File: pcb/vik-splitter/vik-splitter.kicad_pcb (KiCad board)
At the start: 2 copper layers, 25 x 25 mm, 7 parts

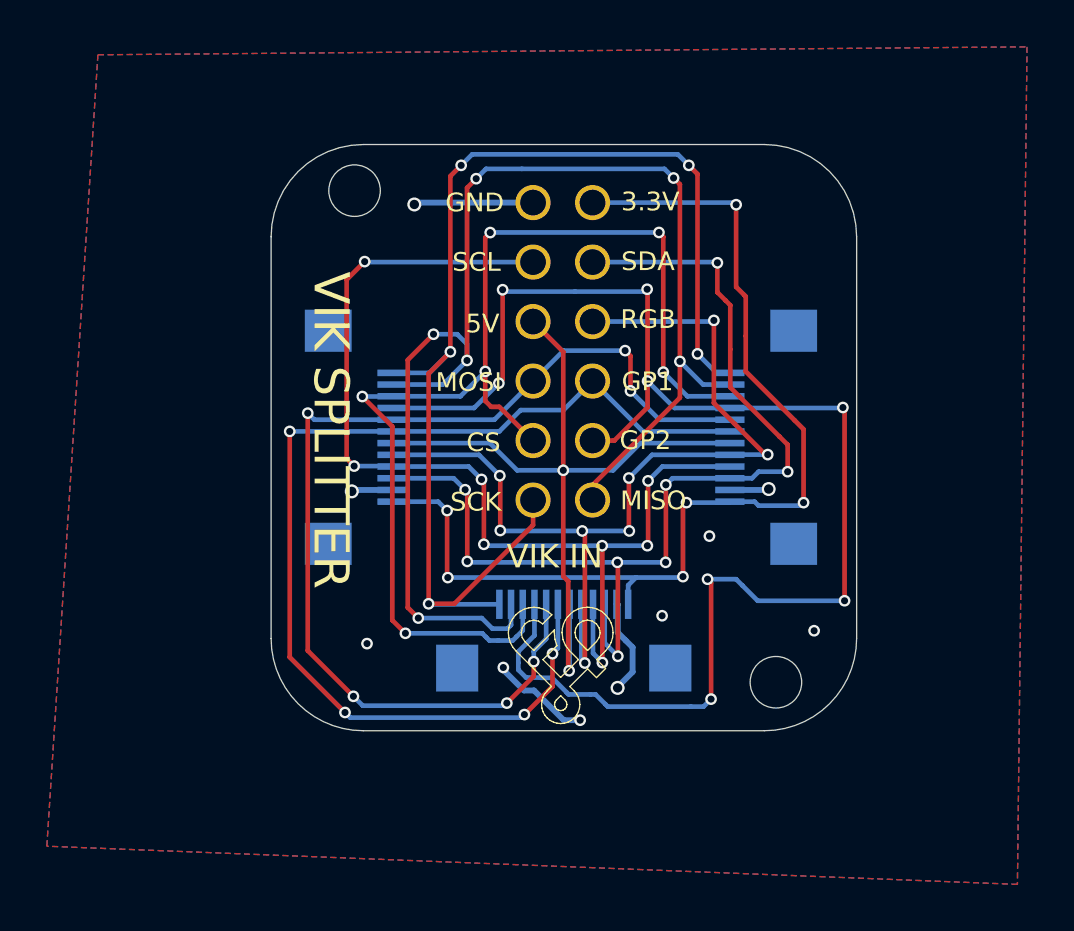
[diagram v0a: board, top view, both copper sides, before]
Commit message: updated vik-splitter footprints and routing to be much cleaner
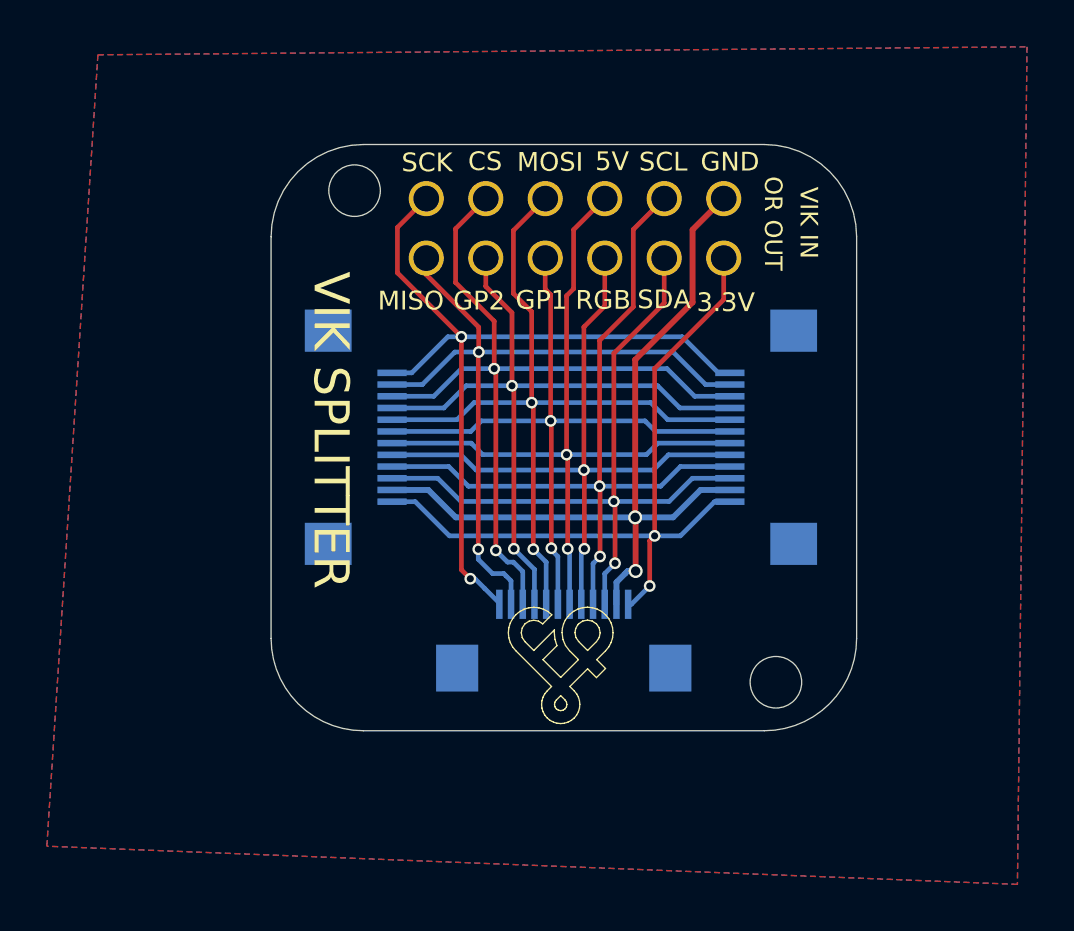
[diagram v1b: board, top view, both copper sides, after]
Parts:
- moved J1002 4.33 mm to (83.4, 101.8), turned to 180 degrees
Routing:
- net GP_AD2_IN: track 63.9 -> 30.9 mm, vias 8 -> 2
- net MISO_IN: track 58.4 -> 32.2 mm, vias 6 -> 2
- net GND: track 16.9 -> 34.8 mm, vias 10 -> 2
- net GP_AD1_IN: track 46.7 -> 29.8 mm, vias 4 -> 2
- net SCLK_IN: track 52.1 -> 35.5 mm, vias 5 -> 2
- net CS_IN: track 49.5 -> 34.6 mm, vias 6 -> 2
- net SDA_IN: track 45.6 -> 31.1 mm, vias 8 -> 2
- net VDD_3.3V_IN: track 45.2 -> 32.2 mm, vias 6 -> 2
- net MOSI_IN: track 46.0 -> 33.5 mm, vias 6 -> 2
- net SCL_IN: track 46.0 -> 33.7 mm, vias 8 -> 2
- net RGB_IN: track 41.6 -> 30.2 mm, vias 8 -> 2
- net VDD_5V_IN: track 33.8 -> 32.9 mm
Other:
- board text added: "OR OUT"
